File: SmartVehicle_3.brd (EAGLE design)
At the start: 87 x 67.4 mm, 129 parts, among them IC1 MPU6050, IC3 ESP8266EX, IC4 24AA32ASN, IC5 TPS77001, IC6 7805T, IC8 TPS77001, J1 U.FL, J3 U.FL, J4 78646-3001, K10 G6A-234P, K6 G6A-234P, K7 G6A-234P, K8 G6A-234P, K9 G6A-234P, Q1 IRF520, Q2 ABM8-26MHz, T10 2N7002, T6 2N7002, T7 2N7002, T8 2N7002, T9 2N7002, U2 MPR121QR2, U3 NEO-6M-GPS, U4 SIM800L, X1 22-23-2021, X10 sign, X11 sign, X12 sign, X8 sign, X9 sign

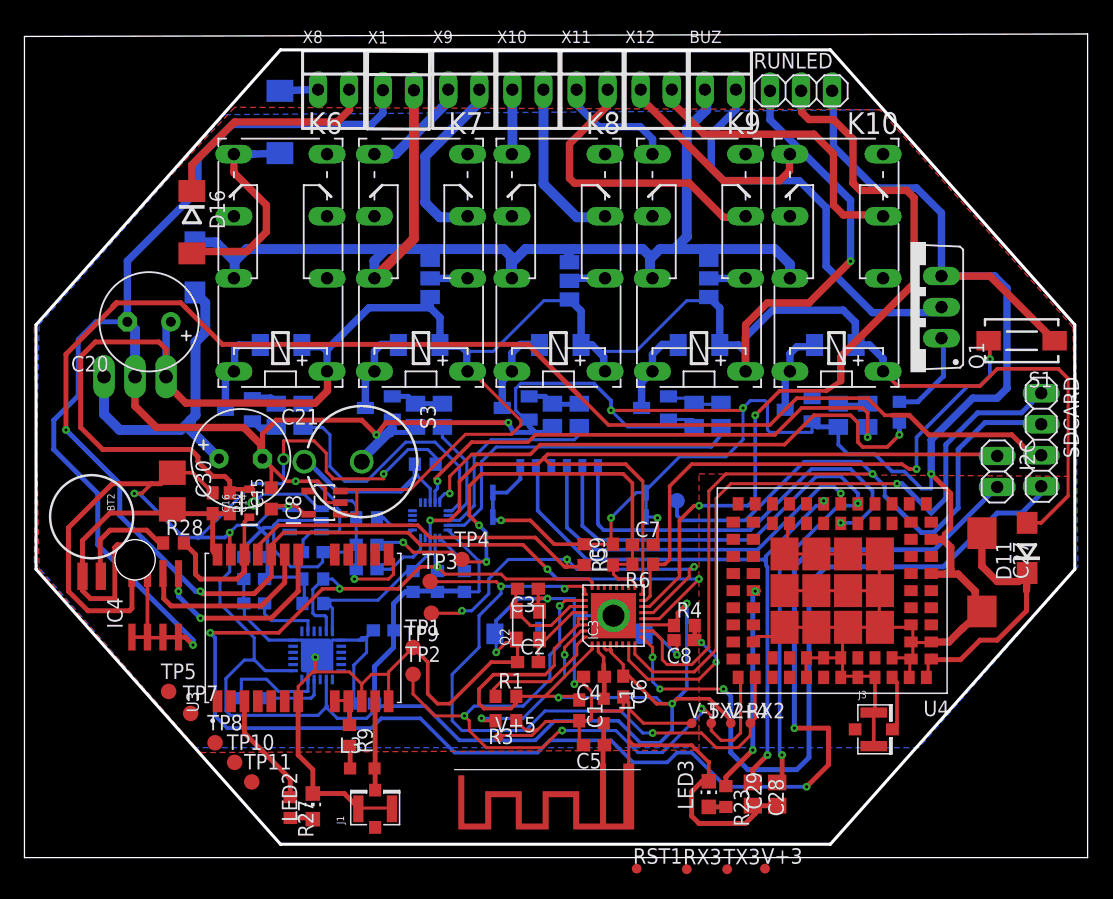
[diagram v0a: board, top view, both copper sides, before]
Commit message: update menambahkan Pin dang menghilangkan Gyro
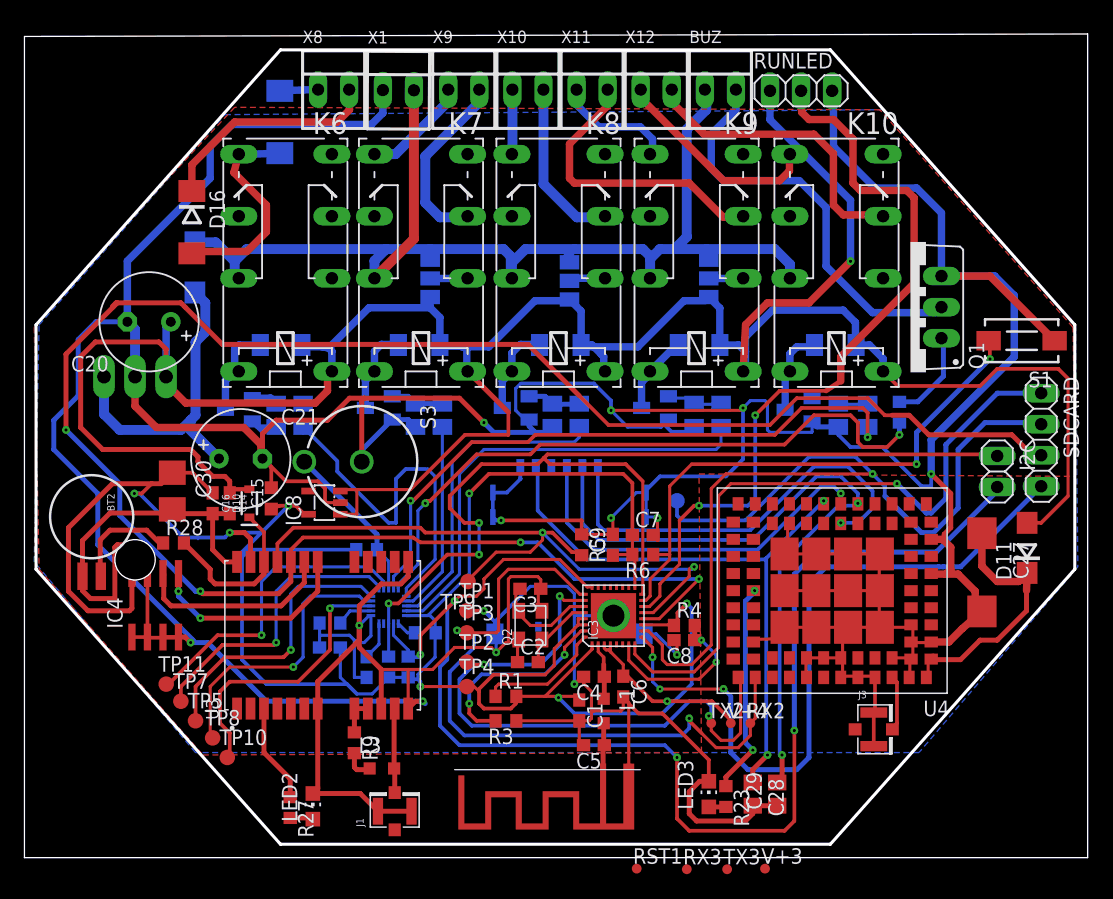
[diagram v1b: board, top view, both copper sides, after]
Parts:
- removed C10, C11, C13: 0.1uF/16V, rcl:C0603
- removed C12: 2200pF, rcl:C0603
- removed C31: 4.7uF/16V, rcl:C0603
- removed C32: 10uF, rcl:C0603
- removed C33: 0.1uF, rcl:C0603
- removed IC1: MPU6050, mpu6050:QFN50P400X400X95-25T265X275N
- removed IC5: TPS77001, texas:SOT23-DBV
- removed R2, R7: 4.7K 1%, resistor:R0603
- removed V+5, V-5: PTR1TP08R, testpad:TP08R
- moved TP11 10.6 mm to (49.4, 34.6)
- moved TP4 10.4 mm to (74.0, 34.4)
- moved R29 9.11 mm to (62.8, 39.6)
- moved C19 8.92 mm to (62.8, 37.6)
- moved R11 8.49 mm to (65.8, 45.6), turned to 0 degrees
- moved C17 8.00 mm to (65.8, 36.0), turned to 270 degrees
- moved U2 7.78 mm to (67.6, 41.0)
- moved R18 7.40 mm to (69.2, 36.0)
- moved R8 7.28 mm to (67.6, 36.0)
- moved TP1 5.33 mm to (74.0, 40.6)
- moved R19 5.28 mm to (70.6, 38.8), turned to 180 degrees
- moved TP3 5.16 mm to (74.0, 38.8)
- moved TP2 4.51 mm to (74.0, 36.4)
- moved TP9 3.97 mm to (74.1, 43.0)
- moved TP5 3.26 mm to (51.8, 31.6)
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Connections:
- removed net N$7: C11.1, IC1.10
- removed net N$8: C12.2, IC1.20
- net +3V3: no longer C10.2, C13.2, C32.2, C33.2, IC1.13, IC1.8, IC5.5, R2.1, R7.1
- net +5V: no longer C31.2, IC5.1, IC5.3
- net GND: no longer C10.1, C11.2, C12.1, C13.1, C31.1, C32.1, C33.1, IC1.1, IC1.11, IC1.18, IC1.25, IC5.2, V+5.TP, V-5.TP
- net IO4: no longer IC1.24, R7.2
- net IO5: no longer IC1.23, R2.2
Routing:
- net +3V3: track 293.7 -> 214.7 mm, vias 11 -> 8
- net IO5: track 145.3 -> 110.4 mm, vias 5 -> 4
- net GND: track 642.2 -> 615.1 mm, vias 16 -> 14
- net N$22: track 0.00 -> 25.4 mm, vias 0 -> 1
- net N$31: track 0.00 -> 24.1 mm, vias 0 -> 1
- net N$30: track 0.00 -> 23.6 mm, vias 0 -> 1
- net N$15: track 0.00 -> 23.2 mm, vias 0 -> 1
- net N$9: track 0.00 -> 23.1 mm, vias 0 -> 1
- net +5V: track 235.9 -> 221.3 mm, vias 2 -> 1
- net REL3: track 16.6 -> 26.0 mm
- net REL4: track 28.4 -> 37.6 mm
- net REL5: track 43.1 -> 51.3 mm
- net BUZZER: track 45.0 -> 53.2 mm
- net REL1: track 23.0 -> 30.0 mm
- net REL2: track 9.04 -> 15.8 mm
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
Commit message: menambahkan via di pin
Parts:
- moved TP10 0.28 mm to (54.6, 28.8)
- moved TP5 0.20 mm to (51.8, 31.8)
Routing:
- net N$9: track 23.1 -> 22.8 mm, vias 1 -> 2
- net N$30: track 23.6 -> 23.4 mm, vias 1 -> 2
- net N$31: vias 1 -> 2
- net N$22: vias 1 -> 2
- net N$15: vias 1 -> 2
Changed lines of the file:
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@@
 <grid distance="0.2" unitdist="mm" unit="mm" style="lines" multiple="1" display="yes" altdistance="0.025" altunitdist="inch" altunit="inch"/>
 <layers>
-<layer number="1" name="Top" color="4" fill="1" visible="yes" active="yes"/>
+<layer number="1" name="Top" color="4" fill="1" visible="no" active="yes"/>
 <layer number="2" name="Route2" color="1" fill="3" visible="no" active="no"/>
 <layer number="3" name="Route3" color="4" fill="3" visible="no" active="no"/>
@@
 <attribute name="TP_SIGNAL_NAME" value="" x="74" y="34.4" size="1.778" layer="27" display="off"/>
 </element>
-<element name="TP5" library="testpad" package="B1,27" value="TPB1,27" x="51.8" y="31.6">
-<attribute name="TP_SIGNAL_NAME" value="" x="51.8" y="31.6" size="1.778" layer="27" display="off"/>
+<element name="TP5" library="testpad" package="B1,27" value="TPB1,27" x="51.8" y="31.8">
+<attribute name="TP_SIGNAL_NAME" value="" x="51.8" y="31.8" size="1.778" layer="27" display="off"/>
 </element>
 <element name="TP7" library="testpad" package="B1,27" value="TPB1,27" x="50.6" y="33.2">
@@
 <attribute name="TP_SIGNAL_NAME" value="" x="53.2" y="30.2" size="1.778" layer="27" display="off"/>
 </element>
-<element name="TP10" library="testpad" package="B1,27" value="TPB1,27" x="54.4" y="28.6">
-<attribute name="TP_SIGNAL_NAME" value="" x="54.4" y="28.6" size="1.778" layer="27" display="off"/>
+<element name="TP10" library="testpad" package="B1,27" value="TPB1,27" x="54.6" y="28.8">
+<attribute name="TP_SIGNAL_NAME" value="" x="54.6" y="28.8" size="1.778" layer="27" display="off"/>
 </element>
 <element name="TP11" library="testpad" package="B1,27" value="TPB1,27" x="49.4" y="34.6">
@@
 <wire x1="58" y1="52.328" x2="57.278" y2="53.05" width="0.3048" layer="1"/>
 <polygon width="0.254" layer="1">
-<vertex x="52.4" y="28.8"/>
+<vertex x="52.6" y="28.8"/>
 <vertex x="93.2" y="29"/>
 <vertex x="93" y="51.8"/>
@@
 <vertex x="124" y="44.2"/>
 <vertex x="111" y="29"/>
-<vertex x="51.8" y="29"/>
+<vertex x="78.2" y="28.8"/>
+<vertex x="70.6" y="28.8"/>
+<vertex x="70.6" y="22"/>
+<vertex x="59.6" y="21.8"/>
+<vertex x="58.8" y="21.8"/>
+<vertex x="58.8" y="22.2"/>
+<vertex x="54.4" y="27"/>
+<vertex x="55.6" y="27.4" curve="90"/>
+<vertex x="55.8" y="29.6"/>
+<vertex x="50.2" y="35.8"/>
+<vertex x="49.6" y="36" curve="90"/>
+<vertex x="47.8" y="34.4"/>
+<vertex x="47.2" y="34.8"/>
 <vertex x="38.6" y="44.6"/>
 </polygon>
@@
 <contactref element="U2" pad="8"/>
 <contactref element="TP10" pad="TP"/>
-<wire x1="54.4" y1="28.6" x2="54.6" y2="28.8" width="0.3048" layer="1"/>
 <wire x1="54.6" y1="28.8" x2="54.6" y2="30.6" width="0.3048" layer="1"/>
 <wire x1="54.6" y1="30.6" x2="53.8" y2="31.4" width="0.3048" layer="1"/>
@@
 <wire x1="60.2" y1="34.8" x2="62.8" y2="37.4" width="0.3048" layer="1"/>
 <wire x1="62.8" y1="37.4" x2="62.8" y2="40.8" width="0.3048" layer="1"/>
+<via x="54.6" y="28.8" extent="1-16" drill="0.8" diameter="1.27"/>
 </signal>
 <signal name="N$13">
@@
 <wire x1="58.4" y1="44.2" x2="57.2" y2="43" width="0.254" layer="16"/>
 <wire x1="57.2" y1="43" x2="57.2" y2="38.6" width="0.254" layer="16"/>
+<via x="49.4" y="34.6" extent="1-16" drill="0.8" diameter="1.27"/>
 </signal>
 <signal name="N$11">
@@
 <wire x1="61.2" y1="41.8" x2="65.2" y2="41.8" width="0.254" layer="16"/>
 <wire x1="60.6" y1="41.2" x2="61.2" y2="41.8" width="0.254" layer="16"/>
+<via x="53.2" y="30.2" extent="1-16" drill="0.8" diameter="1.27"/>
 </signal>
 <signal name="N$30">
 <contactref element="U2" pad="10"/>
 <contactref element="TP5" pad="TP"/>
-<wire x1="51.8" y1="31.6" x2="51.8" y2="34.4" width="0.3048" layer="1"/>
+<wire x1="51.8" y1="31.8" x2="51.8" y2="34.4" width="0.3048" layer="1"/>
 <wire x1="66.1522" y1="41.7874" x2="65.3396" y2="42.6" width="0.254" layer="16"/>
 <via x="59.6" y="37.4" extent="1-16" drill="0.25"/>
@@
 <wire x1="60.2" y1="42.6" x2="59.6" y2="42" width="0.254" layer="16"/>
 <wire x1="59.6" y1="42" x2="59.6" y2="37.4" width="0.254" layer="16"/>
+<via x="51.8" y="31.8" extent="1-16" drill="0.8" diameter="1.27"/>
 </signal>
 <signal name="N$31">
@@
 <wire x1="59.6" y1="43.4" x2="58.4" y2="42.2" width="0.254" layer="16"/>
 <wire x1="58.4" y1="42.2" x2="58.4" y2="38" width="0.254" layer="16"/>
+<via x="50.6" y="33.2" extent="1-16" drill="0.8" diameter="1.27"/>
 </signal>
 </signals>

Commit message: menambahkan battery dan fix GPS
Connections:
- removed net N$56: K7.O1, X9.2
- removed net N$59: K7.S2, X9.1
- new net N$32: K7.S1, X9.2
- net +12V: now also X1.1; no longer X1.2
- net +3V3: now also D10.A
- net +5V: no longer D10.A
- net GND: now also X1.2; no longer X1.1
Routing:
- net N$56: track 15.1 -> 0.00 mm
- net N$59: track 8.80 -> 0.00 mm
- net GND: track 615.1 -> 623.0 mm
- net N$32: track 0.00 -> 5.68 mm
- net +5V: track 221.3 -> 217.0 mm
- net N$35: track 0.00 -> 2.80 mm, vias 0 -> 1
- net +3V3: track 214.7 -> 217.5 mm
- net +12V: track 96.1 -> 98.7 mm, vias 0 -> 1

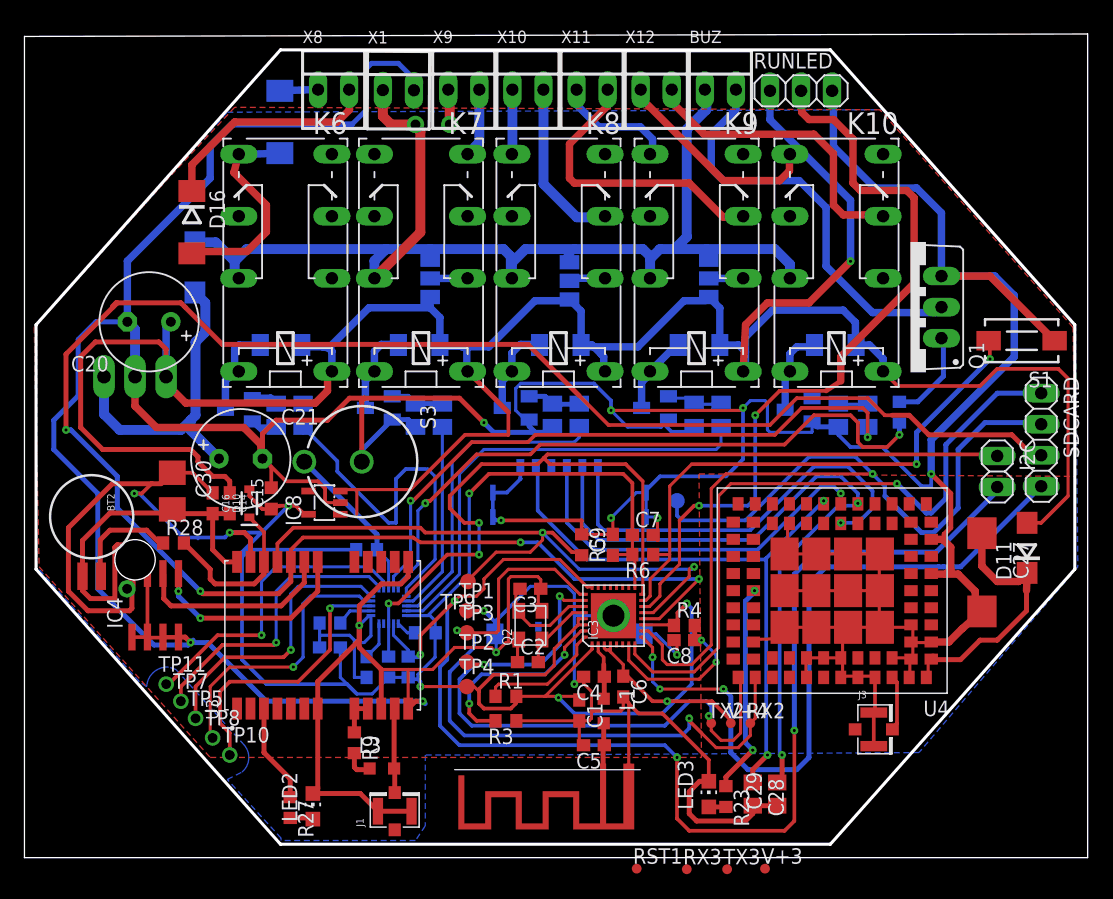
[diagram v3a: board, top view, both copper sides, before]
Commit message: merapihkan jalur yang berdempetan
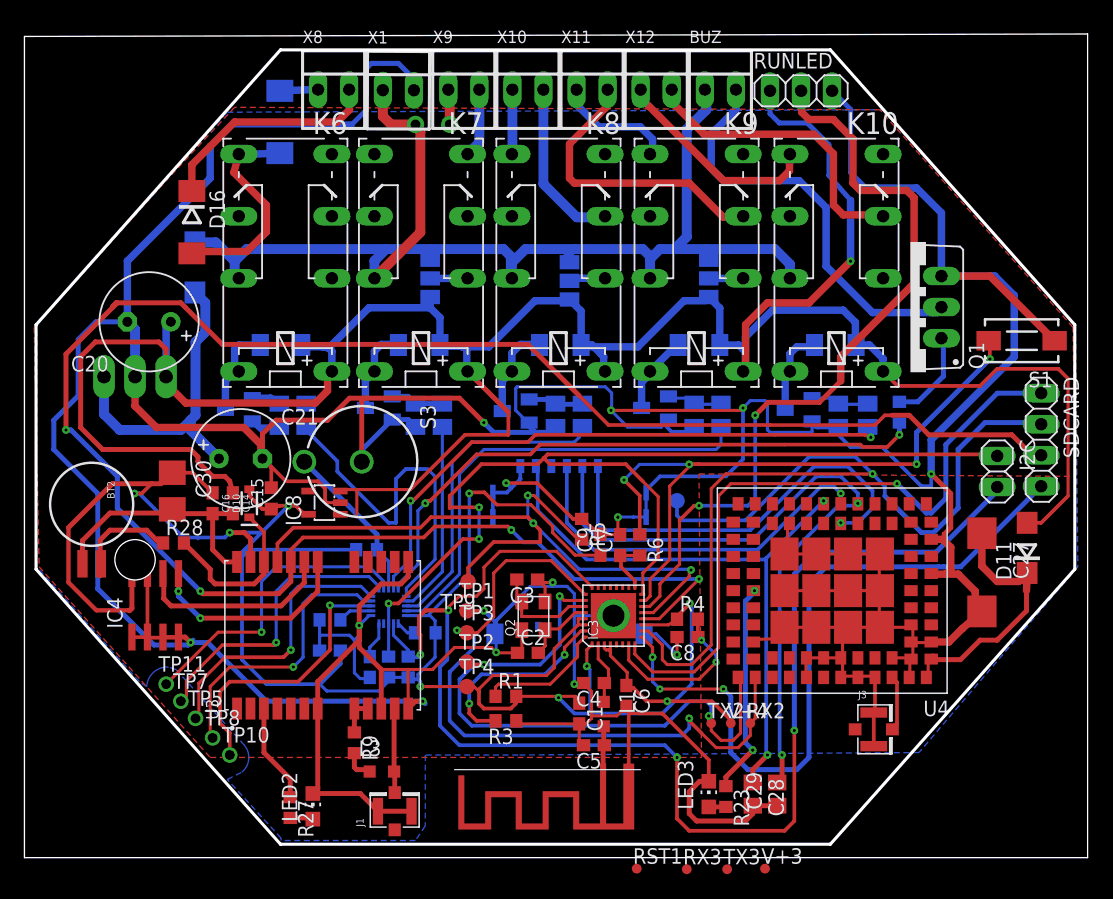
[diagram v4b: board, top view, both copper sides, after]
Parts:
- moved C7 2.02 mm to (86.5, 46.0), turned to 90 degrees
- moved R5 1.27 mm to (83.4, 47.3)
- moved BT2 1.02 mm to (43.3, 49.3)
- moved C9 1.02 mm to (84.9, 46.0)
- moved R6 0.82 mm to (88.2, 46.0), turned to 270 degrees
- moved C3 0.80 mm to (78.9, 43.2)
- moved C6 0.80 mm to (87.1, 33.6)
- moved Q2 0.80 mm to (79.5, 40.2)
- moved C2 0.76 mm to (79.0, 37.2)
- moved R4 0.57 mm to (92.1, 39.9)
- moved C4 0.51 mm to (84.4, 34.7)
- moved C8 0.36 mm to (92.1, 38.5)
- moved C1 0.25 mm to (83.2, 32.2)
- moved C17 0.25 mm to (66.1, 36.0)
- moved C19 0.25 mm to (62.8, 37.3)
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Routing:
- net GND: track 623.0 -> 595.9 mm
- net IO0: track 45.4 -> 55.7 mm, vias 2 -> 4
- net +3V3: track 217.5 -> 210.2 mm, vias 8 -> 9
- net IO15: track 55.9 -> 62.2 mm, vias 2 -> 3
- net BUZZER: track 53.2 -> 50.3 mm
- net REL5: track 51.3 -> 48.6 mm
- net IO5: track 110.4 -> 111.7 mm
- net +5V: track 217.0 -> 218.3 mm
- net IO4: track 84.3 -> 85.4 mm
- net N$52: track 8.91 -> 9.80 mm
- net N$61: track 5.08 -> 5.91 mm
- net N$35: track 2.80 -> 2.04 mm
- net N$4: track 4.82 -> 5.58 mm
- net N$3: track 6.48 -> 5.92 mm
